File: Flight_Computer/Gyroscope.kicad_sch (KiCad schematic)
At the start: 70 parts, among them J1 SWD, J10 Motor, J2 TYPE-C-31-M-12, J3 I2C, J4 5V, J5 GND, J6 AMT102, J7 FC_RF, J9 AMT102, Q1 2N7002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

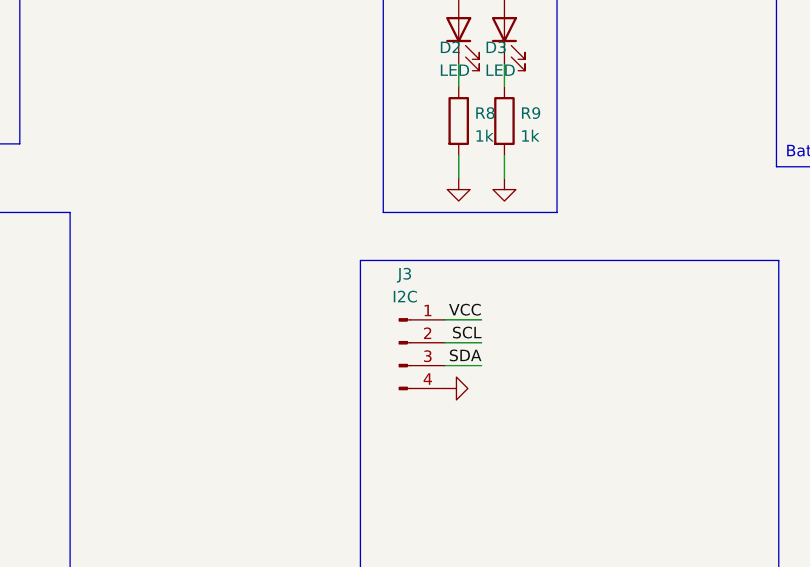
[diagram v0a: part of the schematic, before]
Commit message: added remaining footprints to gyroscope schematic and starting laying out components on PCB
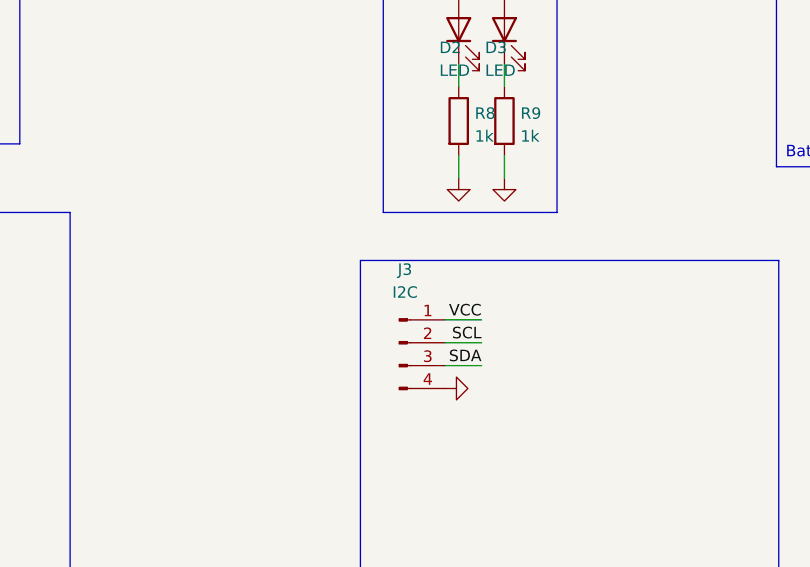
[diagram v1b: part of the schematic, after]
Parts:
- J10: footprint (none) -> Connector_PinHeader_2.54mm:PinHeader_1x02_P2.54mm_Vertical
- J3: footprint (none) -> Connector_PinHeader_2.54mm:PinHeader_1x04_P2.54mm_Vertical
- J6, J9: footprint (none) -> Connector_PinHeader_2.54mm:PinHeader_1x05_P2.54mm_Vertical
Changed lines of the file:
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@@
 	(wire
 		(pts
+			(xy 45.72 208.28) (xy 57.15 208.28)
+		)
+		(stroke
+			(width 0)
+			(type default)
+		)
+	)
+	(wire
+		(pts
 			(xy 369.824 220.726) (xy 378.46 220.726)
 		)
@@
 	(wire
 		(pts
-			(xy 45.72 208.28) (xy 57.15 208.28)
-		)
-		(stroke
-			(width 0)
-			(type default)
-		)
-	)
-	(wire
-		(pts
 			(xy 113.538 48.26) (xy 113.538 49.53)
 		)
@@
 		(fields_autoplaced yes)
 		(property "Reference" "J3"
-			(at 120.269 192.278 0)
+			(at 120.269 191.77 0)
 			(effects
 				(font
@@
 		)
 		(property "Value" "I2C"
-			(at 120.269 194.818 0)
+			(at 120.269 194.31 0)
 			(effects
 				(font
@@
 			)
 		)
-		(property "Footprint" ""
+		(property "Footprint" "Connector_PinHeader_2.54mm:PinHeader_1x04_P2.54mm_Vertical"
 			(at 119.634 199.898 0)
 			(effects
@@
 			)
 		)
-		(property "Footprint" ""
+		(property "Footprint" "Connector_PinHeader_2.54mm:PinHeader_1x02_P2.54mm_Vertical"
 			(at 276.86 77.47 0)
 			(effects
@@
 			)
 		)
-		(property "Footprint" ""
+		(property "Footprint" "Connector_PinHeader_2.54mm:PinHeader_1x05_P2.54mm_Vertical"
 			(at 304.8 34.29 0)
 			(effects
@@
 			)
 		)
-		(property "Footprint" ""
+		(property "Footprint" "Connector_PinHeader_2.54mm:PinHeader_1x05_P2.54mm_Vertical"
 			(at 306.07 83.82 0)
 			(effects
